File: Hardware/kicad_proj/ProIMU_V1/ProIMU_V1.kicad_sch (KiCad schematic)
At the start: 31 parts, among them J1 USB4105-GF-A, J2 502570-0893, U1 BMP280, U2 MPU-9250, U3 STM32F412CEU6, U4 AIR602, U5 POGOPIN, U6 POGOPIN, U7 POGOPIN, U8 POGOPIN, U9 POGOPIN

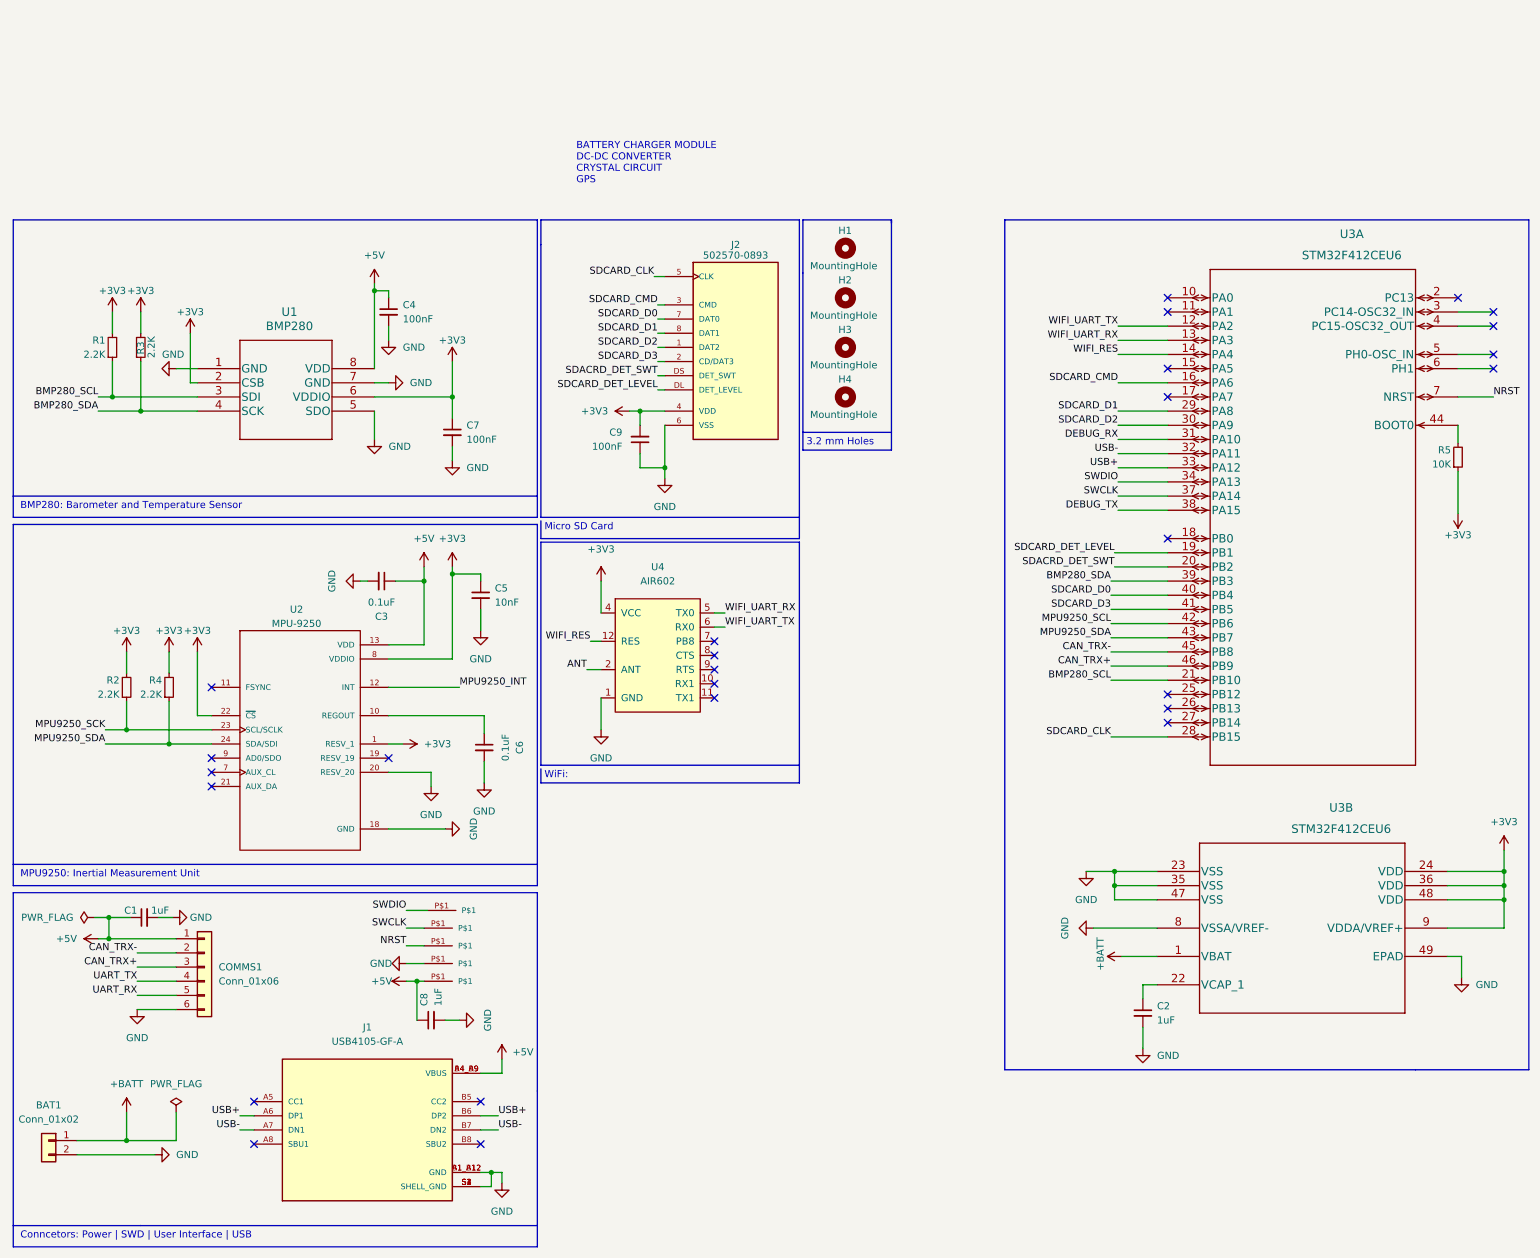
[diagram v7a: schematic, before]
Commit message: Update: Layout updated. Pinout needs to be revised
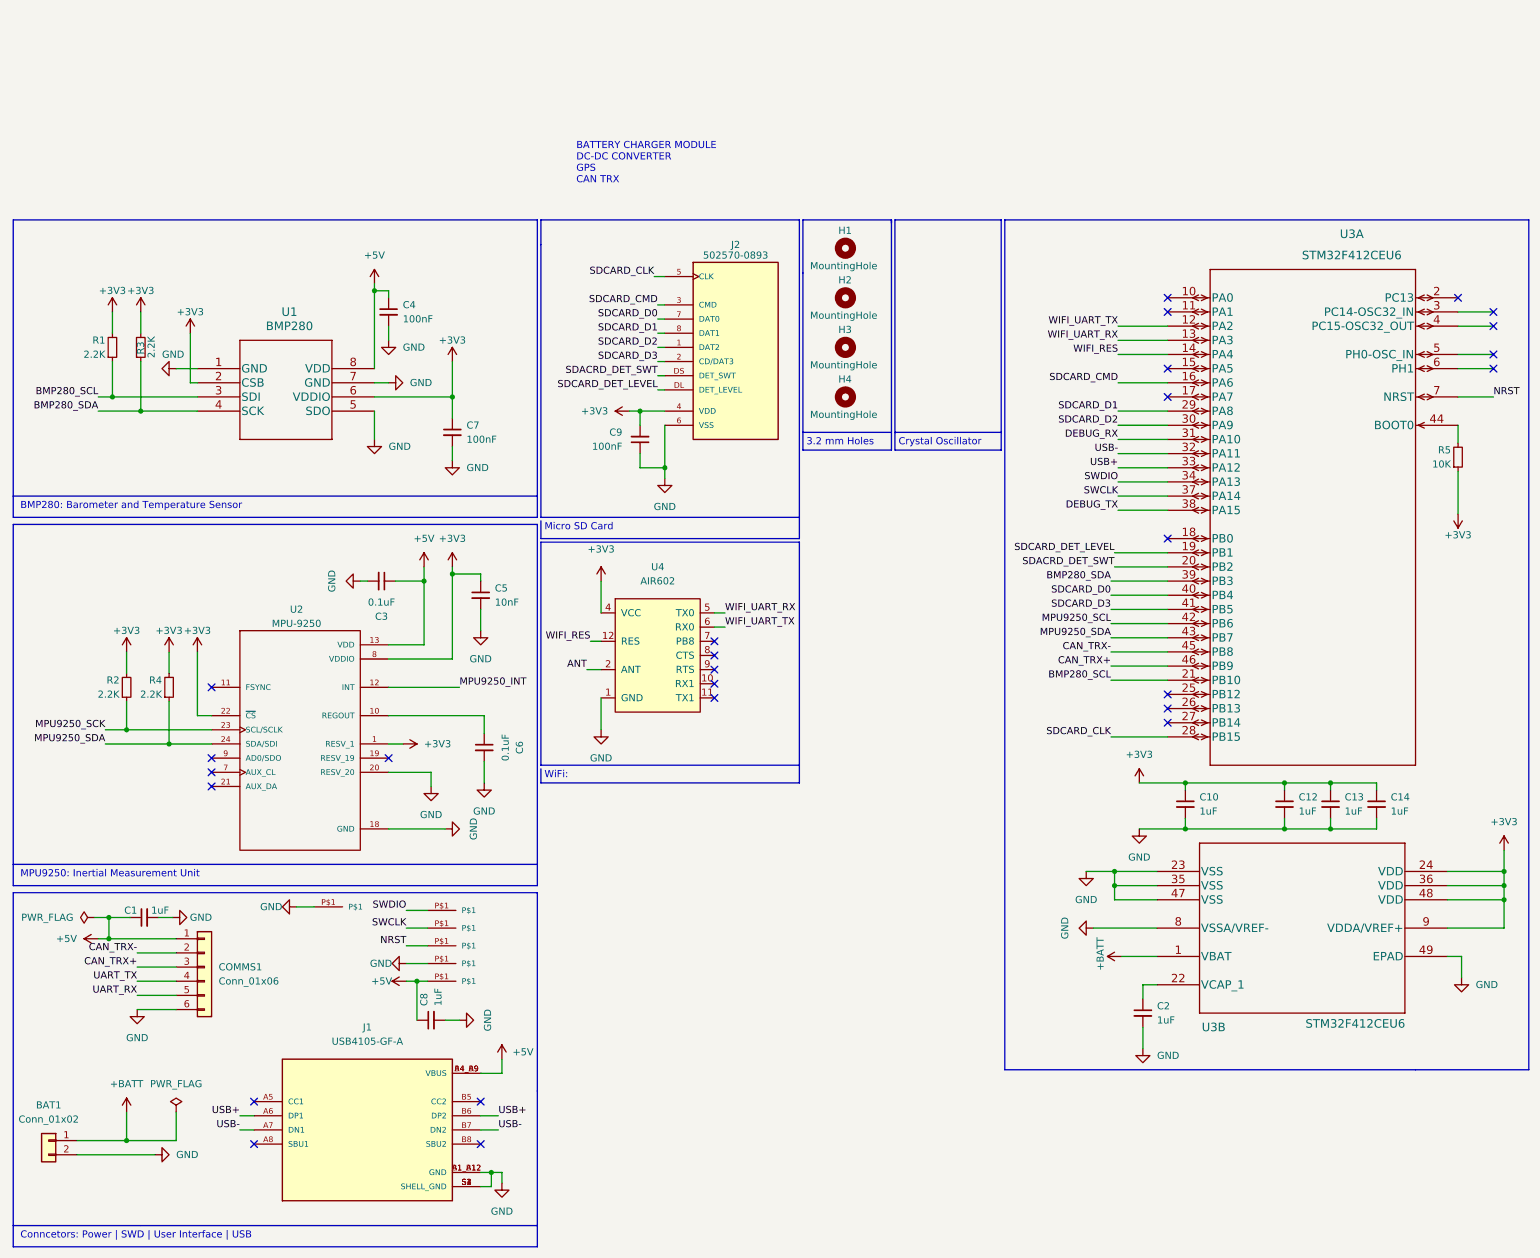
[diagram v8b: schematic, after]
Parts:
- added C10, C12, C13, C14: 1uF, Capacitor_SMD:C_0402_1005Metric_Pad0.74x0.62mm_HandSolder, symbol Device:C_Small
- added U10: POGOPIN, footprints:Test_Point, symbol POGOPIN:POGOPIN
- U5, U6, U7, U8, U9: footprint footprints:1.27MM_POGO -> footprints:Test_Point
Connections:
- net +3V3: now also C10.1, C12.1, C13.1, C14.1
- net +5V: now also U10.P$1; no longer U9.P$1
- net GND: now also U5.P$1, U9.P$1, C10.2, C12.2, C13.2, C14.2; no longer U8.P$1
- net NRST: now also U8.P$1; no longer U7.P$1
- net SWCLK: now also U7.P$1; no longer U5.P$1
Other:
- note added: "BATTERY CHARGER MODULE DC-DC CONVERTER GPS CAN TRX"
- note added: "Crystal Oscillator"
- note removed: "BATTERY CHARGER MODULE DC-DC CONVERTER CRYSTAL CIRCUIT GPS"
